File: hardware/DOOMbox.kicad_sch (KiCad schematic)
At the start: 37 parts, among them J1 DE15_Socket_HighDensity, J2 AudioJack3, SW1 SW_SPST, SW2 SW_Push, U1 RPi Pico 2, U2 MCP23S08, U3 AP7381-50SA-7, U4 LM324N, U5 CD4010BE

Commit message: Some PWM programming and testing to play a C note
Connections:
- net at RV1.2: now also U4.12 (+); no longer U4.10 (+)
- net at RV2.2: now also U4.10 (+); no longer U4.12 (+)
- new net: C4.1, U4.13 (-), U4.14
- new net: C12.1, U4.8, U4.9 (-)
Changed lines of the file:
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@@
 		(at 212.09 41.91 0)
 		(mirror x)
-		(unit 3)
+		(unit 4)
 		(exclude_from_sim no)
 		(in_bom yes)
@@
 				(path "/eddfbb36-34c6-4c43-a971-b4c3a9c38a8f"
 					(reference "U4")
-					(unit 3)
+					(unit 4)
 				)
 			)
@@
 		(at 212.09 68.58 0)
 		(mirror x)
-		(unit 4)
+		(unit 3)
 		(exclude_from_sim no)
 		(in_bom yes)
@@
 				(path "/eddfbb36-34c6-4c43-a971-b4c3a9c38a8f"
 					(reference "U4")
-					(unit 4)
-				)
-			)
+					(unit 3)
+				)
+			)

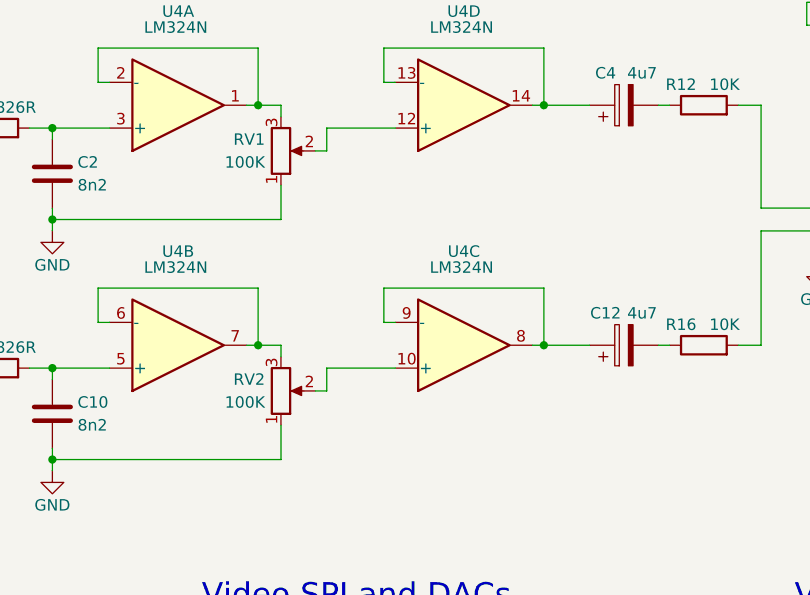
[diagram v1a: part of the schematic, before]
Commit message: Some PWM notes added to schematic
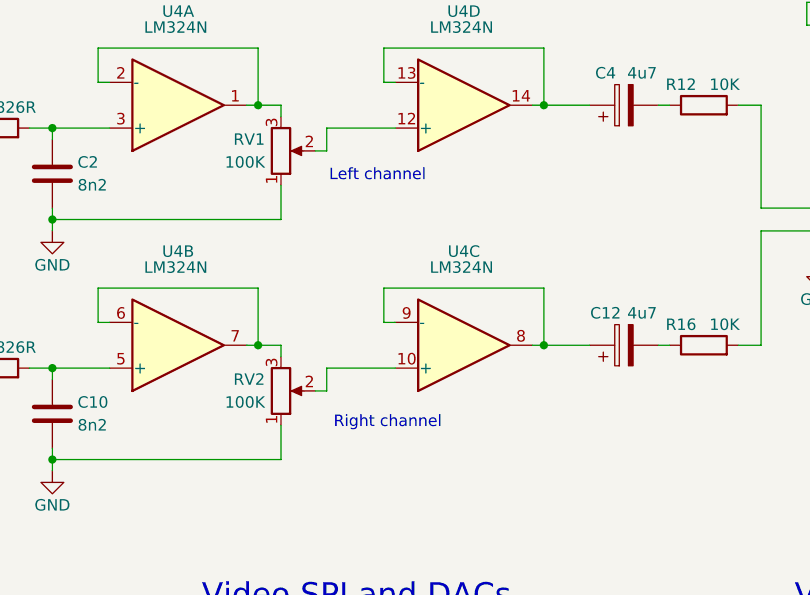
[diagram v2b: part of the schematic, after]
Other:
- note added: "Left channel"
- note added: "Right channel"
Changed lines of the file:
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@@
 		(company "Jack Bennett")
+	)
+	(text "Left channel"
+		(exclude_from_sim no)
+		(at 197.104 49.784 0)
+		(effects
+			(font
+				(size 1.27 1.27)
+				(color 0 0 255 1)
+			)
+			(justify left)
+		)
 	)
 	(text "Video SPI and DACs"
@@
 		(effects
 			(font
+				(size 1.27 1.27)
+				(color 0 0 255 1)
+			)
+			(justify left)
+		)
+	)
+	(text "Right channel"
+		(exclude_from_sim no)
+		(at 197.612 77.216 0)
+		(effects
+			(font

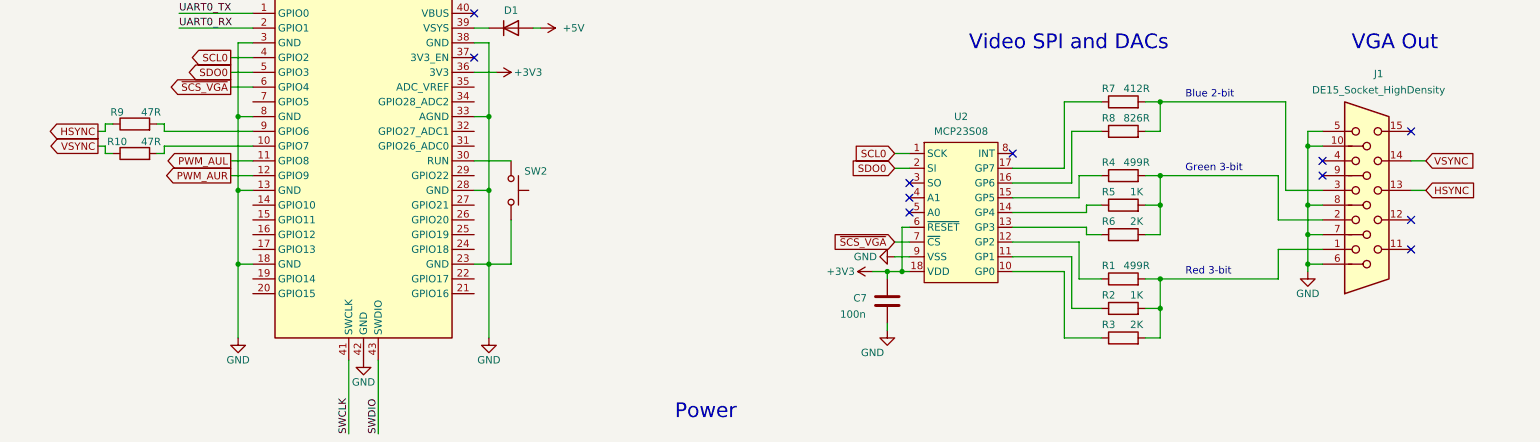
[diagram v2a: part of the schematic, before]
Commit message: Add starting point of the driver for the onboard buzzer
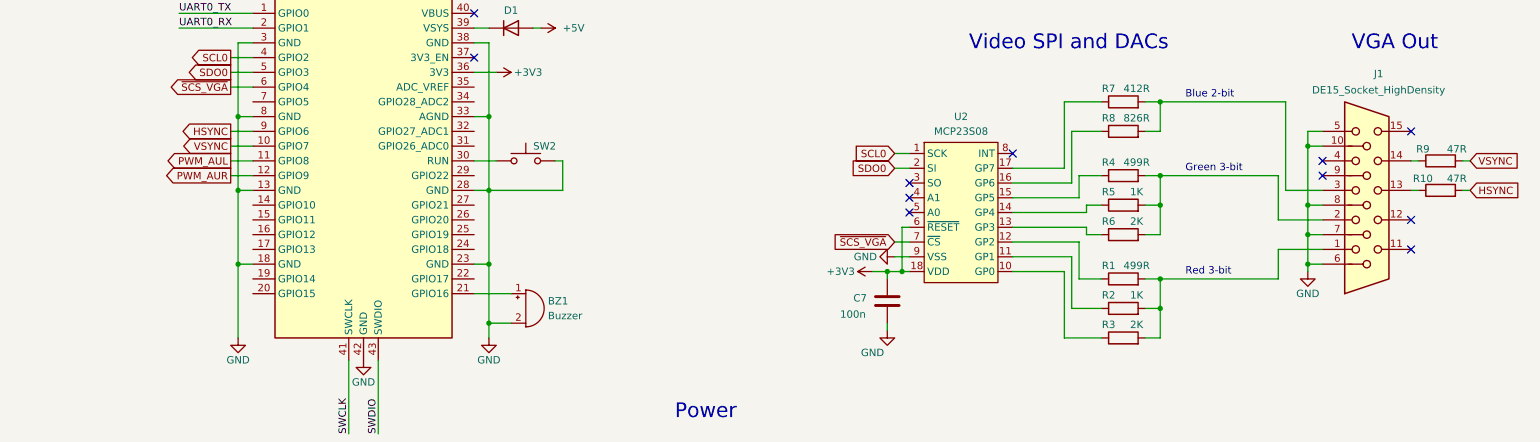
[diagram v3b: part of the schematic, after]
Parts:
- added BZ1: Buzzer, symbol Device:Buzzer
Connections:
- net GND: now also BZ1.2 (-)
- net HSYNC: now also R10.2, U1.9 (GPIO6); no longer J1.13, R9.1
- net VSYNC: now also R9.2, U1.10 (GPIO7); no longer J1.14, R10.1
- net at U1.21 (GPIO16): now also BZ1.1 (+)
- new net: J1.13, R10.1
- new net: J1.14, R9.1
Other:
- moved on the sheet: R10, R9, SW2

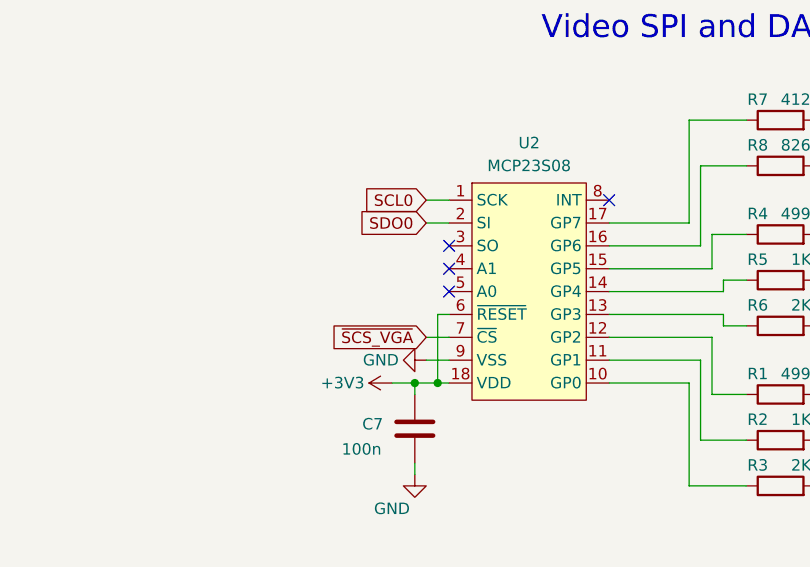
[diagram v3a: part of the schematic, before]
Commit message: SPI testing for VGA (+ fix MCP address pins not tied to GND)
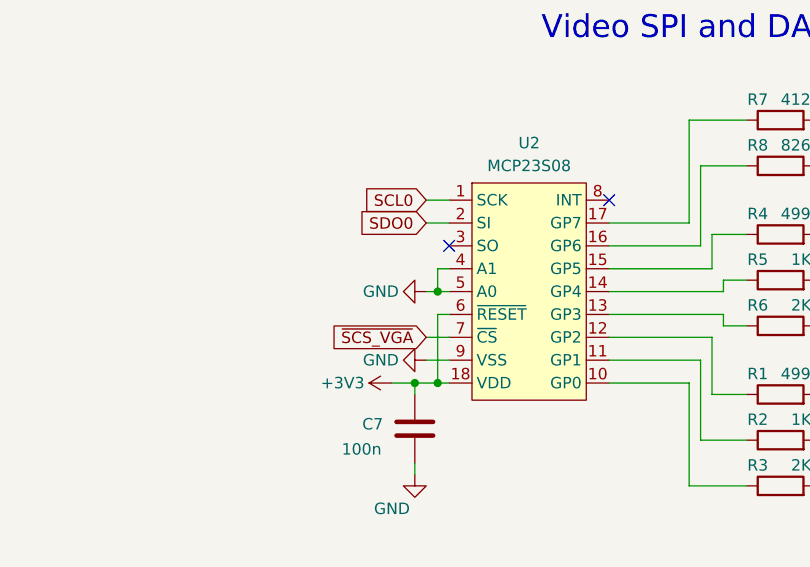
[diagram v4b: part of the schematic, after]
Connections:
- net GND: now also U2.4 (A1), U2.5 (A0)
- no-connect marks 19 -> 17
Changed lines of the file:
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@@
 	)
 	(junction
+		(at 171.45 125.73)
+		(diameter 0)
+		(color 0 0 0 0)
+	)
+	(junction
 		(at 166.37 71.12)
 		(diameter 0)
@@
 	)
 	(no_connect
-		(at 172.72 125.73)
-	)
-	(no_connect
-		(at 172.72 123.19)
-	)
-	(no_connect
 		(at 139.7 58.42)
 	)
@@
 	(wire
 		(pts
+			(xy 171.45 125.73) (xy 172.72 125.73)
+		)
+		(stroke
+			(width 0)
+			(type default)
+		)
+	)
+	(wire
+		(pts
 			(xy 166.37 81.28) (xy 191.77 81.28)
 		)
@@
 	(wire
 		(pts
+			(xy 172.72 123.19) (xy 171.45 123.19)
+		)
+		(stroke
+			(width 0)
+			(type default)
+		)
+	)
+	(wire
+		(pts
 			(xy 241.3 111.76) (xy 241.3 114.3)
 		)
@@
 	(wire
 		(pts
+			(xy 171.45 123.19) (xy 171.45 125.73)
+		)
+		(stroke
+			(width 0)
+			(type default)
+		)
+	)
+	(wire
+		(pts
 			(xy 245.11 68.58) (xy 245.11 55.88)
 		)
@@
 	(wire
 		(pts
+			(xy 170.18 125.73) (xy 171.45 125.73)
+		)
+		(stroke
+			(width 0)
+			(type default)
+		)
+	)
+	(wire
+		(pts
 			(xy 236.22 119.38) (xy 236.22 127)
 		)
@@
 					(unit 1)
 				)
+			)
+		)
+	)
+	(symbol
+		(lib_id "power:GND")
+		(at 170.18 125.73 270)
+		(unit 1)
+		(exclude_from_sim no)
+		(in_bom yes)
+		(on_board yes)
+		(dnp no)
+		(property "Reference" "#PWR016"
+			(at 163.83 125.73 0)
+			(effects
+				(font
+					(size 1.27 1.27)
+				)
+				(hide yes)
+			)
+		)
+		(property "Value" "GND"
+			(at 167.132 125.73 90)
+			(effects
+				(font
+					(size 1.27 1.27)
+				)
+				(justify right)
+			)
+		)
+		(property "Footprint" ""
+			(at 170.18 125.73 0)
+			(effects
+				(font
+					(size 1.27 1.27)
+				)
+				(hide yes)
+			)
+		)
+		(property "Datasheet" ""
+			(at 170.18 125.73 0)
+			(effects
+				(font
+					(size 1.27 1.27)
+				)
+				(hide yes)
+			)
+		)
+		(property "Description" "Power symbol creates a global label with name \"GND\" , ground"
+			(at 170.18 125.73 0)
+			(effects
+				(font
+					(size 1.27 1.27)
+				)
+				(hide yes)
+			)
+		)
+		(pin "1"
+		)
+		(instances
+			(project "DOOMbox"
+				(path "/eddfbb36-34c6-4c43-a971-b4c3a9c38a8f"
+					(reference "#PWR016")
+					(unit 1)
+				)

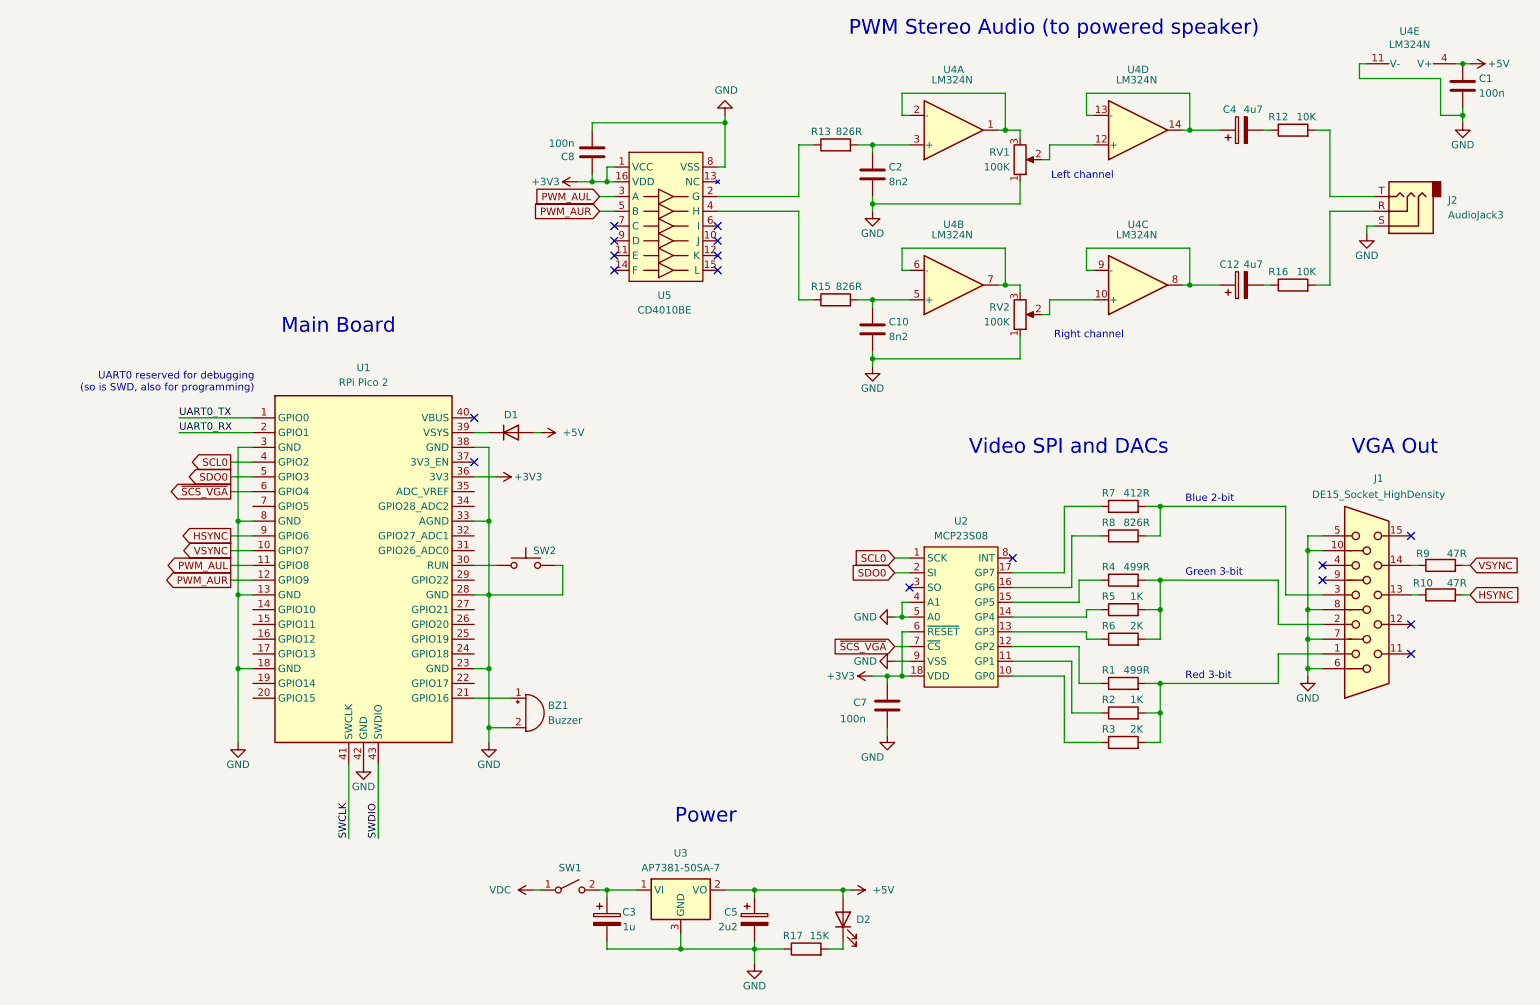
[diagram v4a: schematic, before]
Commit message: Working VGA output direct from Pico (ie. removed MCP23S08) + palette
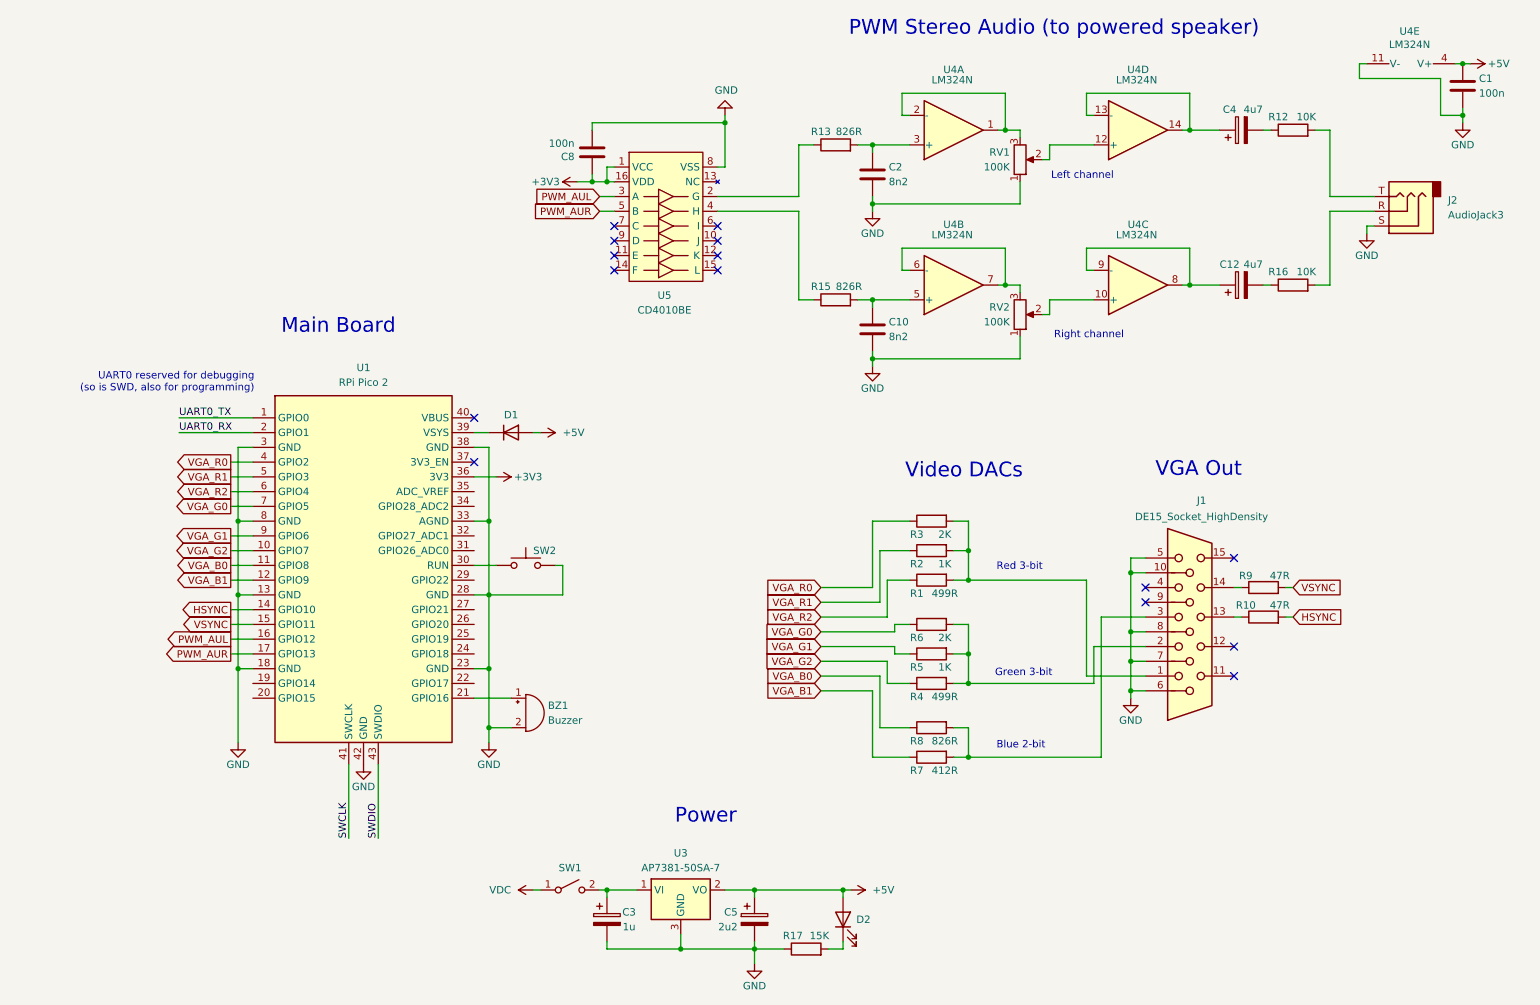
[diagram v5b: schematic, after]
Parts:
- removed C7: 100n, symbol Device:C
- removed U2: MCP23S08, MCU_Microchip_MCP:DIP794W56P254L2286H533Q18N, symbol MCU_Microchip_MCP:MCP23S08
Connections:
- net SCL0 is gone; now on net VGA_R0: U1.4 (GPIO2)
- net SDO0 is gone; now on net VGA_R1: U1.5 (GPIO3)
- net ~{SCS_VGA} is gone; now on net VGA_R2: U1.6 (GPIO4)
- net HSYNC: now also U1.14 (GPIO10); no longer U1.9 (GPIO6)
- net PWM_AUL: now also U1.16 (GPIO12); no longer U1.11 (GPIO8)
- net PWM_AUR: now also U1.17 (GPIO13); no longer U1.12 (GPIO9)
- net VSYNC: now also U1.15 (GPIO11); no longer U1.10 (GPIO7)
- net VGA_R0: now reaches R3.1
- net VGA_R1: now reaches R2.1
- net VGA_R2: now reaches R1.1
- net VGA_G0: now reaches R6.1
- net VGA_G0: now also U1.7 (GPIO5)
- net VGA_G1: now reaches R5.1
- net VGA_G1: now also U1.9 (GPIO6)
- net VGA_G2: now reaches R4.1
- net VGA_G2: now also U1.10 (GPIO7)
- net VGA_B0: now reaches R8.1
- net VGA_B0: now also U1.11 (GPIO8)
- net VGA_B1: now reaches R7.1
- net VGA_B1: now also U1.12 (GPIO9)
- no-connect marks 17 -> 15
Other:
- note added: "Video DACs"
- note removed: "Video SPI and DACs"
- moved on the sheet: J1, R1, R10, R2, R3, R4, R5, R6, R7, R8, R9
